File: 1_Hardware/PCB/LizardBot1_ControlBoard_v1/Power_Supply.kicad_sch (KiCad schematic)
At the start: 7 parts, among them J201 Conn_01x02, Q201 AO3401A, SW201 SW_Push, SW202 SW_SPST

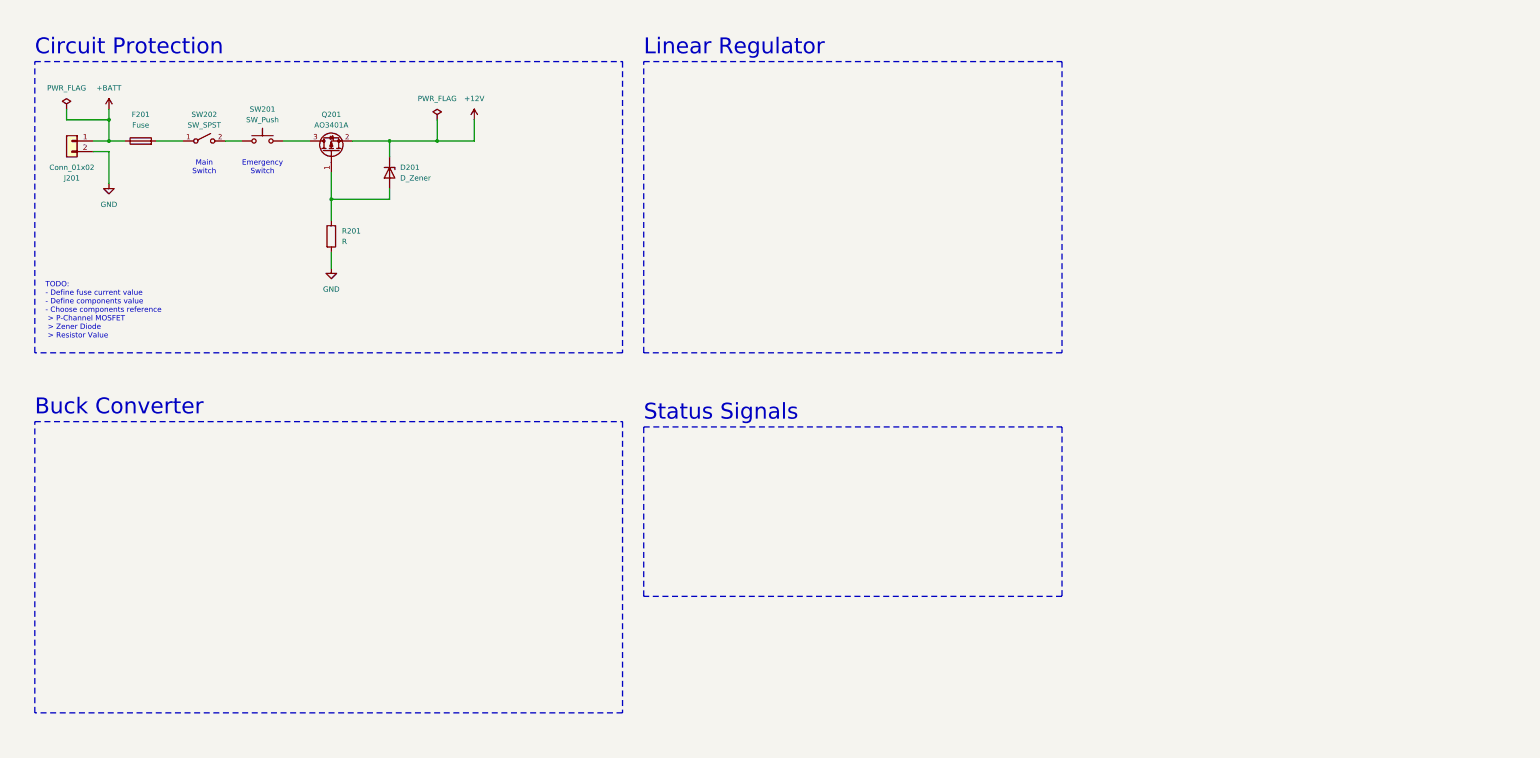
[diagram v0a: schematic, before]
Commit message: Updated Electrical Layout Block Diagram. Added Power_Supply schematic last changes.
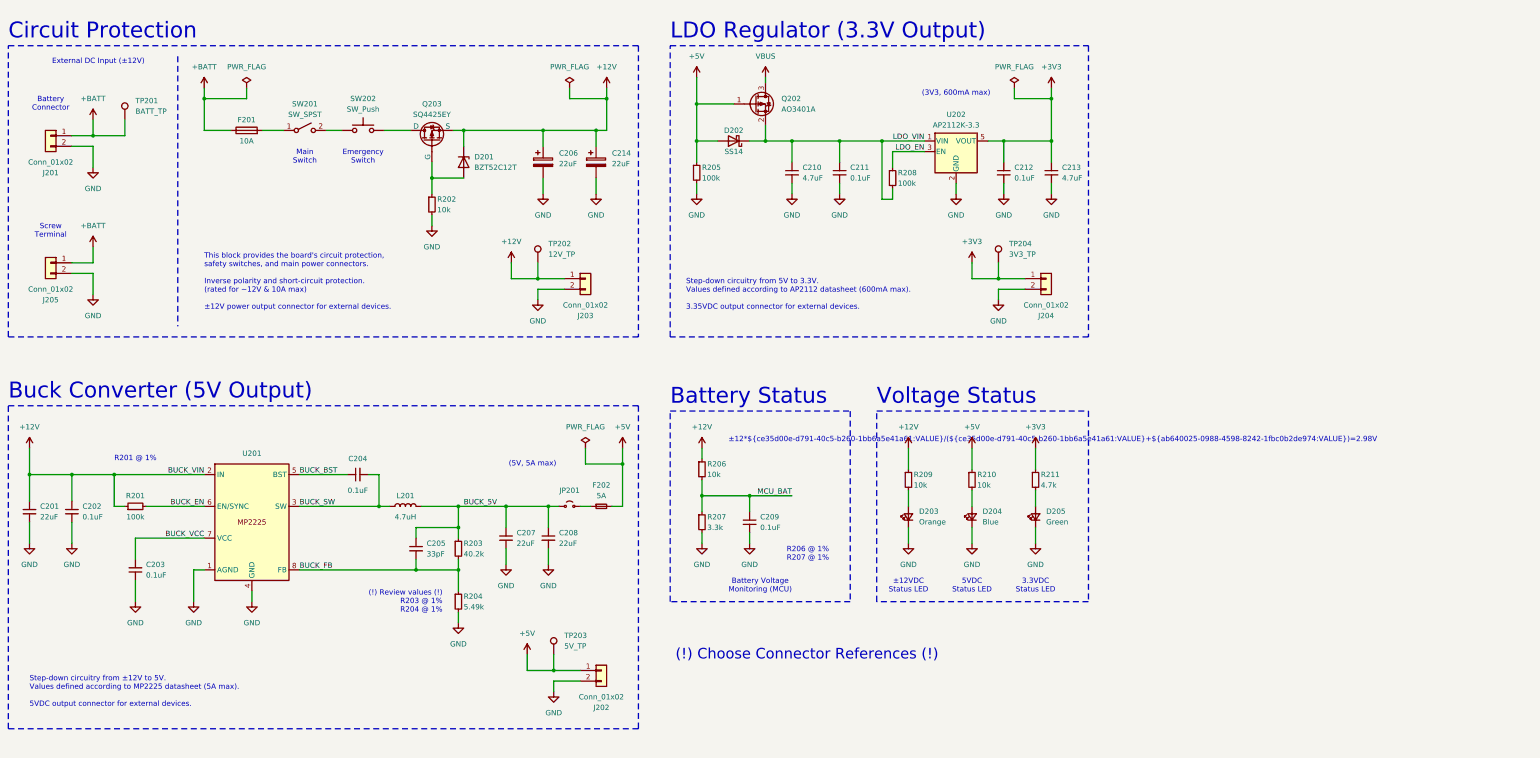
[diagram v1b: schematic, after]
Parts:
- removed Q201: AO3401A, Package_TO_SOT_SMD:SOT-23, symbol Transistor_FET:AO3401A
- added C201, C207, C208: 22uF, symbol Device:C_Small
- added C202, C203, C204, C209, C211, C212: 0.1uF, symbol Device:C_Small
- added C205: 33pF, symbol Device:C_Small
- added C206, C214: 22uF, symbol Device:C_Polarized
- added C210, C213: 4.7uF, symbol Device:C_Small
- added D202: SS14, symbol Device:D_Schottky
- added D203: Orange, symbol Device:LED_Small
- added D204: Blue, symbol Device:LED_Small
- added D205: Green, symbol Device:LED_Small
- added F202: 5A, symbol Device:Fuse_Small
- added J202, J203, J204, J205: Conn_01x02, symbol Connector_Generic:Conn_01x02
- added JP201: Jumper_2_Small_Open, symbol Jumper:Jumper_2_Small_Open
- added L201: 4.7uH, symbol Device:L
- added Q202: AO3401A, Package_TO_SOT_SMD:SOT-23, symbol Transistor_FET:AO3401A
- added Q203: SQ4425EY, Package_SO:SO-8_3.9x4.9mm_P1.27mm, symbol Simulation_SPICE:PMOS
- added R201, R205, R208: 100k, symbol Device:R_Small
- added R203: 40.2k, symbol Device:R_Small
- added R204: 5.49k, symbol Device:R_Small
- added R206, R209, R210: 10k, symbol Device:R_Small
- added R207: 3.3k, symbol Device:R_Small
- added R211: 4.7k, symbol Device:R_Small
- added TP201: BATT_TP, symbol Connector:TestPoint
- added TP202: 12V_TP, symbol Connector:TestPoint
- added TP203: 5V_TP, symbol Connector:TestPoint
- added TP204: 3V3_TP, symbol Connector:TestPoint
- added U201: ~, Package_TO_SOT_SMD:SOT-23-8, symbol PowerSupply_Symbols:MP2225
- added U202: AP2112K-3.3, Package_TO_SOT_SMD:SOT-23-5, symbol Regulator_Linear:AP2112K-3.3
- D201: value D_Zener -> BZT52C12T
- F201: value Fuse -> 10A
- R202: renamed from R201; value R -> 10k; symbol Device:R -> Device:R_Small
- renumbered SW202 to SW201, SW201 to SW202
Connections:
- net +12V: now also C201.1, C202.1, C206.1, C214.1, J203.1 (Pin_1), Q203.1 (S), Q203.2 (S), Q203.3 (S), R201.1, R206.1, R209.1, TP202.1, U201.2 (IN)
- net +BATT: now also J205.1 (Pin_1), TP201.1
- net GND: now also C201.2, C202.2, C203.2, C206.2, C207.2, C208.2, C209.2, C210.2, C211.2, C212.2, C213.2, C214.2, D203.1 (K), D204.1 (K), D205.1 (K), J202.2 (Pin_2), J203.2 (Pin_2), J204.2 (Pin_2), J205.2 (Pin_2), R204.2, R205.2, R207.2, U201.1 (AGND), U201.4 (GND), U202.2 (GND)
- net at D201.2 (A), R202.1: now also Q203.4 (G)
- net at SW202.2: now also Q203.5 (D), Q203.6 (D), Q203.7 (D), Q203.8 (D)
- new net: D203.2 (A), R209.2
- new net: D204.2 (A), R210.2
- new net: D205.2 (A), R211.2
- new net: F202.1, JP201.2 (B)
- new net +3V3: C212.1, C213.1, J204.1 (Pin_1), R211.1, TP204.1, U202.5 (VOUT)
- new net +5V: D202.2 (A), F202.2, J202.1 (Pin_1), Q202.1 (G), R205.1, R210.1, TP203.1
- new net BUCK_5V: C205.1, C207.1, C208.1, JP201.1 (A), L201.2, R203.1
- new net BUCK_BST: C204.1, U201.5 (BST)
- new net BUCK_EN: R201.2, U201.6 (EN/SYNC)
- new net BUCK_FB: C205.2, R203.2, R204.1, U201.8 (FB)
- new net BUCK_SW: C204.2, L201.1, U201.3 (SW)
- new net BUCK_VCC: C203.1, U201.7 (VCC)
- new net LDO_EN: R208.1, U202.3 (EN)
- new net LDO_VIN: C210.1, C211.1, D202.1 (K), Q202.2 (S), R208.2, U202.1 (VIN)
- new net MCU_BAT: C209.1, R206.2, R207.1
- new net VBUS: Q202.3 (D)
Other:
- note added: "(!) Choose Connector References (!)"
- note added: "(!) Review values (!) R203 @ 1% R204 @ 1%"
- note added: "(3V3, 600mA max)"
- note added: "(5V, 5A max)"
- note added: "3.3VDC Status LED"
- note added: "5VDC Status LED"
- note added: "Battery Connector"
- note added: "Battery Status"
- note added: "Battery Voltage Monitoring (MCU)"
- note added: "Buck Converter (5V Output)"
- note added: "External DC Input (±12V)"
- note added: "LDO Regulator (3.3V Output)"
- note added: "R201 @ 1%"
- note added: "R206 @ 1% R207 @ 1%"
- note added: "Screw Terminal"
- note added: "Step-down circuitry from 5V to 3.3V. Values defined according to AP2112 datasheet (600mA max). 3.35VDC output connector for external devices."
- note added: "Step-down circuitry from ±12V to 5V. Values defined according to MP2225 datasheet (5A max). 5VDC output connector for external devices."
- note added: "This block provides the board's circuit protection, safety switches, and main power connectors. Inverse polarity and short-circuit protection. (rated for ~12V & 10A max) ±12V power output connector for external devices."
- note added: "Voltage Status"
- note added: "±12*${ce35d00e-d791-40c5-b260-1bb6a5e41a61:VALUE}/(${ce35d00e-d791-40c5-b260-1bb6a5e41a61:VALUE}+${ab640025-0988-4598-8242-1fbc0b2de974:VALUE})=2.98V"
- note added: "±12VDC Status LED"
- note removed: "Buck Converter"
- note removed: "Linear Regulator"
- note removed: "Status Signals"
- note removed: "TODO: - Define fuse current value - Define components value - Choose components reference > P-Channel MOSFET > Zener Diode > Resistor Value"
- moved on the sheet: D201, F201, J201, R202, SW201, SW202

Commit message: Added Motor_Driver schematic.
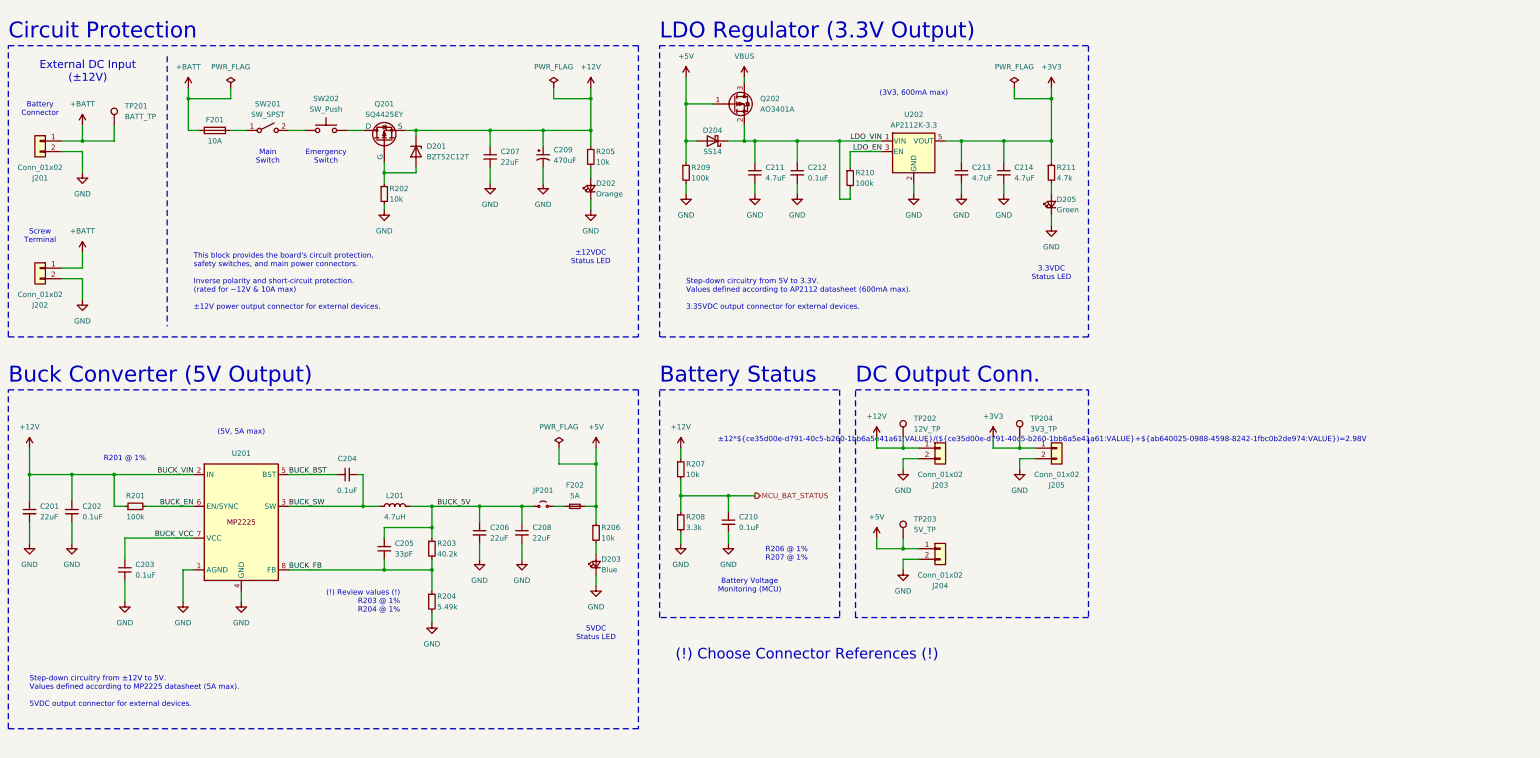
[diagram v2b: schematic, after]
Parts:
- removed C206, C214: 22uF, symbol Device:C_Polarized
- removed C212: 0.1uF, symbol Device:C_Small
- removed D204: Blue, symbol Device:LED_Small
- removed R209, R210: 10k, symbol Device:R_Small
- removed U201: ~, Package_TO_SOT_SMD:SOT-23-8, symbol PowerSupply_Symbols:MP2225
- added C207: 22uF, symbol Device:C_Small
- added C209: 470uF, symbol Device:C_Polarized_Small_US
- added C214: 4.7uF, symbol Device:C_Small
- added D202: Orange, symbol Device:LED_Small
- added R205, R206: 10k, symbol Device:R_Small
- added U201: ~, Package_TO_SOT_SMD:SOT-23-8, symbol Project_SymbolLib:MP2225
- D203: value Orange -> Blue
- renumbered C207 to C206, C209 to C210, C210 to C211, C211 to C212, D202 to D204, J205 to J202, J202 to J204, J204 to J205, Q203 to Q201, R206 to R207, R207 to R208, R205 to R209, R208 to R210
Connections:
- net +12V: now also C207.1, C209.1, R205.1, U201.2 (IN); no longer Q201.1 (S), Q201.2 (S)
- net +3V3: now also C214.1
- net +5V: now also R206.1
- net BUCK_BST: now also U201.5 (BST)
- net BUCK_EN: now also U201.6 (EN/SYNC)
- net BUCK_FB: now also U201.8 (FB)
- net BUCK_SW: now also U201.3 (SW)
- net BUCK_VCC: now also U201.7 (VCC)
- net GND: now also C207.2, C209.2, C214.2, D202.1 (K), U201.1 (AGND), U201.4 (GND)
- net at D203.2 (A): now also R206.2
- net at D201.2 (A), R202.1: now also Q201.2 (G); no longer Q201.4 (G)
- net MCU_BAT renamed MCU_BAT_STATUS
- new net: Q201.1 (D), SW202.2
- new net: D202.2 (A), R205.2
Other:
- note added: "DC Output Conn."
- note removed: "Voltage Status"
- moved on the sheet: C203, C204, C206, C208, C210, C211, C212, D201, D204, F201, F202, J201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

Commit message: Added MCU schematic
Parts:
- removed J202: Conn_01x02, symbol Connector_Generic:Conn_01x02
- added J202: Screw_Terminal_01x02, symbol Connector:Screw_Terminal_01x02
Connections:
- net +BATT: now also J202.2 (Pin_2)
- net GND: now also J202.1 (Pin_1)
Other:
- note added: "(!) Needs Final Review (!) Step-down circuitry from 5V to 3.3V. Values defined according to AP2112 datasheet (600mA max). 3.35VDC output connector for external devices."
- note removed: "Step-down circuitry from 5V to 3.3V. Values defined according to AP2112 datasheet (600mA max). 3.35VDC output connector for external devices."
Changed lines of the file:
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@@
 	(title_block
 		(title "LizardBot 1 Control Board: Power Supply")
-		(date "2024-06-21")
+		(date "2024-06-10")
 		(rev "v1.0.0")
 		(company "Lizard Electronics")
@@
 	(wire
 		(pts
-			(xy 36.83 49.53) (xy 36.83 54.61)
+			(xy 44.45 49.53) (xy 44.45 53.34)
 		)
 		(stroke
@@
 	(wire
 		(pts
-			(xy 31.75 49.53) (xy 36.83 49.53)
+			(xy 31.75 49.53) (xy 44.45 49.53)
 		)
 		(stroke
@@
 	(wire
 		(pts
-			(xy 31.75 80.01) (xy 36.83 80.01)
+			(xy 31.75 80.01) (xy 44.45 80.01)
 		)
 		(stroke
@@
 	(wire
 		(pts
-			(xy 36.83 80.01) (xy 36.83 85.09)
+			(xy 44.45 80.01) (xy 44.45 85.09)
 		)
 		(stroke
@@
 		)
 	)
-	(text "Step-down circuitry from 5V to 3.3V.\nValues defined according to AP2112 datasheet (600mA max).\n\n3.35VDC output connector for external devices."
+	(text "(!) Needs Final Review (!)\nStep-down circuitry from 5V to 3.3V.\nValues defined according to AP2112 datasheet (600mA max).\n\n3.35VDC output connector for external devices."
 		(exclude_from_sim no)
 		(at 181.61 87.63 0)
@@
 	)
 	(symbol
+		(lib_id "Connector:Screw_Terminal_01x02")
+		(at 26.67 80.01 180)
+		(unit 1)
+		(exclude_from_sim no)
+		(in_bom yes)
+		(on_board yes)
+		(dnp no)
+		(property "Reference" "J202"
+			(at 25.4 74.93 0)
+			(effects
+				(font
+					(size 1.27 1.27)
+				)
+				(justify right)
+			)
+		)
+		(property "Value" "Screw_Terminal_01x02"
+			(at 25.4 82.55 0)
+			(effects
+				(font
+					(size 1.27 1.27)
+				)
+				(justify right)
+			)
+		)
+		(property "Footprint" ""
+			(at 26.67 80.01 0)
+			(effects
+				(font
+					(size 1.27 1.27)
+				)
+				(hide yes)
+			)
+		)
+		(property "Datasheet" "~"
+			(at 26.67 80.01 0)
+			(effects
+				(font
+					(size 1.27 1.27)
+				)
+				(hide yes)
+			)
+		)
+		(property "Description" "Generic screw terminal, single row, 01x02, script generated (kicad-library-utils/schlib/autogen/connector/)"
+			(at 26.67 80.01 0)
+			(effects
+				(font
+					(size 1.27 1.27)
+				)
+				(hide yes)
+			)
+		)
+		(pin "1"
+		)
+		(pin "2"
+		)
+		(instances
+			(project ""
+				(path "/1a674a4d-d877-4d7a-ad57-e0a054705c31/1ad8e535-9964-46ac-bb04-941393eb127d"
+					(reference "J202")
+					(unit 1)
+				)
+			)
+		)
+	)
+	(symbol
 		(lib_id "power:GND")
 		(at 257.81 59.69 0)
@@
 	)
 	(symbol
-		(lib_id "Connector_Generic:Conn_01x02")
-		(at 26.67 77.47 0)
-		(mirror y)
-		(unit 1)
-		(exclude_from_sim no)
-		(in_bom yes)
-		(on_board yes)
-		(dnp no)
-		(property "Reference" "J202"
-			(at 26.67 86.36 0)
-			(effects
-				(font
-					(size 1.27 1.27)
-				)
-			)
-		)
-		(property "Value" "Conn_01x02"
-			(at 26.67 83.82 0)
-			(effects
-				(font
-					(size 1.27 1.27)
-				)
-			)
-		)
-		(property "Footprint" ""
-			(at 26.67 77.47 0)
-			(effects
-				(font
-					(size 1.27 1.27)
-				)
-				(hide yes)
-			)
-		)
-		(property "Datasheet" "~"
-			(at 26.67 77.47 0)
-			(effects
-				(font
-					(size 1.27 1.27)
-				)
-				(hide yes)
-			)
-		)
-		(property "Description" "Generic connector, single row, 01x02, script generated (kicad-library-utils/schlib/autogen/connector/)"
-			(at 26.67 77.47 0)
-			(effects
-				(font
-					(size 1.27 1.27)
-				)
-				(hide yes)
-			)
-		)
-		(pin "2"
-		)
-		(pin "1"
-		)
-		(instances
-			(project "LizardBot1_ControlBoard_v1"
-				(path "/1a674a4d-d877-4d7a-ad57-e0a054705c31/1ad8e535-9964-46ac-bb04-941393eb127d"
-					(reference "J202")
-					(unit 1)
-				)
-			)
-		)
-	)
-	(symbol
 		(lib_id "power:GND")
-		(at 36.83 85.09 0)
+		(at 44.45 85.09 0)
 		(unit 1)
 		(exclude_from_sim no)
@@
 		(fields_autoplaced yes)
 		(property "Reference" "#PWR0207"
-			(at 36.83 91.44 0)
+			(at 44.45 91.44 0)
 			(effects
 				(font
@@
 		)
 		(property "Value" "GND"
-			(at 36.83 90.17 0)
+			(at 44.45 90.17 0)
 			(effects
 				(font
@@
 		)
 		(property "Footprint" ""
-			(at 36.83 85.09 0)
+			(at 44.45 85.09 0)
 			(effects
 				(font
@@
 		)
 		(property "Datasheet" ""
-			(at 36.83 85.09 0)
+			(at 44.45 85.09 0)
 			(effects
 				(font
@@
 		)
 		(property "Description" "Power symbol creates a global label with name \"GND\" , ground"
-			(at 36.83 85.09 0)
+			(at 44.45 85.09 0)
 			(effects
 				(font
@@
 		(dnp no)
 		(property "Reference" "J201"
-			(at 26.67 55.88 0)
+			(at 25.4 44.45 0)
 			(effects
 				(font
 					(size 1.27 1.27)
 				)
+				(justify right)
 			)
 		)
 		(property "Value" "Conn_01x02"
-			(at 26.67 53.34 0)
+			(at 25.4 52.07 0)
 			(effects
 				(font
 					(size 1.27 1.27)
 				)
+				(justify right)
 			)
 		)
@@
 	(symbol
 		(lib_id "power:GND")
-		(at 36.83 54.61 0)
+		(at 44.45 53.34 0)
 		(unit 1)
 		(exclude_from_sim no)
@@
 		(dnp no)
 		(fields_autoplaced yes)
-		(property "Reference" "#PWR0205"
-			(at 36.83 60.96 0)
+		(property "Reference" "#PWR0206"
+			(at 44.45 59.69 0)
 			(effects
 				(font
@@
 		)
 		(property "Value" "GND"
-			(at 36.83 59.69 0)
+			(at 44.45 58.42 0)
 			(effects
 				(font
@@
 		)
 		(property "Footprint" ""
-			(at 36.83 54.61 0)
+			(at 44.45 53.34 0)
 			(effects
 				(font
@@
 		)
 		(property "Datasheet" ""
-			(at 36.83 54.61 0)
+			(at 44.45 53.34 0)
 			(effects
 				(font
@@
 		)
 		(property "Description" "Power symbol creates a global label with name \"GND\" , ground"
-			(at 36.83 54.61 0)
+			(at 44.45 53.34 0)
 			(effects
 				(font
@@
 			(project "LizardBot1_ControlBoard_v1"
 				(path "/1a674a4d-d877-4d7a-ad57-e0a054705c31/1ad8e535-9964-46ac-bb04-941393eb127d"
-					(reference "#PWR0205")
+					(reference "#PWR0206")
 					(unit 1)
 				)
@@
 		(dnp no)
 		(fields_autoplaced yes)
-		(property "Reference" "#PWR0206"
+		(property "Reference" "#PWR0205"
 			(at 36.83 77.47 0)
 			(effects
@@
 			(project "LizardBot1_ControlBoard_v1"
 				(path "/1a674a4d-d877-4d7a-ad57-e0a054705c31/1ad8e535-9964-46ac-bb04-941393eb127d"
-					(reference "#PWR0206")
+					(reference "#PWR0205")
 					(unit 1)
 				)
